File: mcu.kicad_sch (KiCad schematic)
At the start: 38 parts, among them IC1 SN74AHCT1G125DBVR, J201 Connector, USB-TYPE-C-16P, SW201 SK-12D02, U1 STM32F723VET6, U2 USBLC6-2SC6, U201 TS3USB221ARSER, X1 16MHz

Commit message: fixes & doc
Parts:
- removed C180: 1uF, PCM_JLCPCB:C_0402, symbol PCM_JLCPCB-Capacitors:0402,1uF
- removed C181: 100nF, PCM_JLCPCB:C_0402, symbol PCM_JLCPCB-Capacitors:0402,100nF

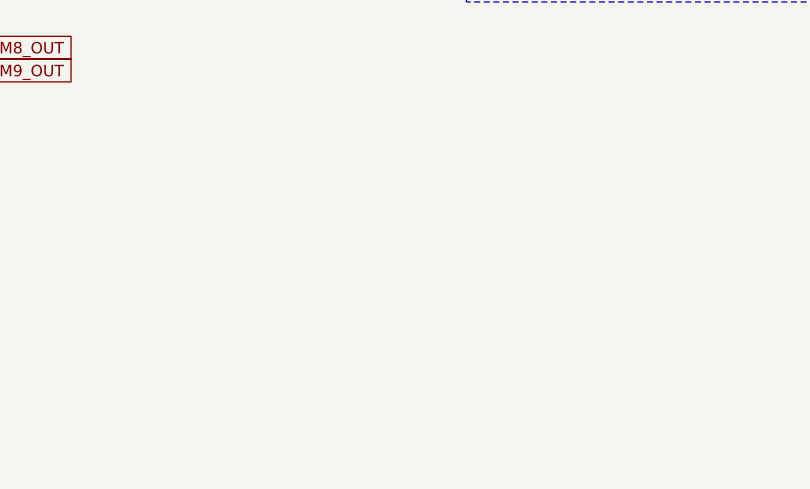
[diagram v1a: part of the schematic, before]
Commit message: Add rotary encoder symbol;
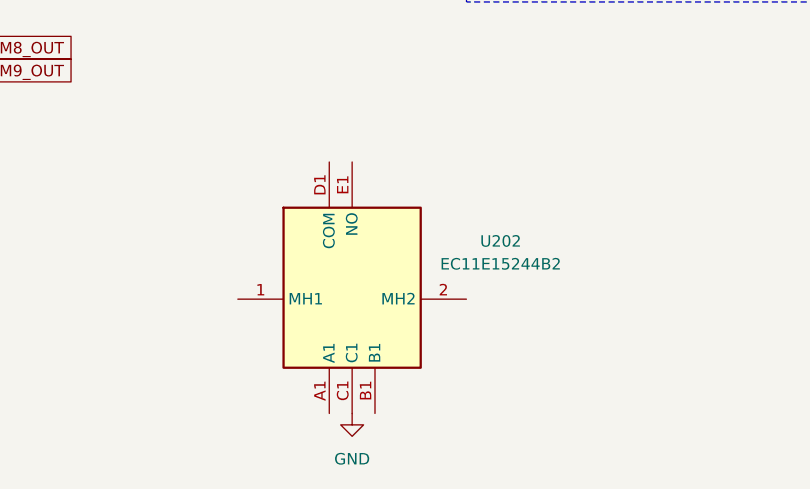
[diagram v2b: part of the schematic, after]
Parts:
- added U202: EC11E15244B2, EC11E15244B2, symbol SamacSys_Parts:EC11E15244B2
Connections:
- net GND: now also U202.C1
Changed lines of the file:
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@@
 	(symbol
 		(lib_id "power:GND")
+		(at 284.48 214.63 0)
+		(unit 1)
+		(exclude_from_sim no)
+		(in_bom yes)
+		(on_board yes)
+		(dnp no)
+		(fields_autoplaced yes)
+		(property "Reference" "#PWR0233"
+			(at 284.48 220.98 0)
+			(effects
+				(font
+					(size 1.27 1.27)
+				)
+				(hide yes)
+			)
+		)
+		(property "Value" "GND"
+			(at 284.48 219.71 0)
+			(effects
+				(font
+					(size 1.27 1.27)
+				)
+			)
+		)
+		(property "Footprint" ""
+			(at 284.48 214.63 0)
+			(effects
+				(font
+					(size 1.27 1.27)
+				)
+				(hide yes)
+			)
+		)
+		(property "Datasheet" ""
+			(at 284.48 214.63 0)
+			(effects
+				(font
+					(size 1.27 1.27)
+				)
+				(hide yes)
+			)
+		)
+		(property "Description" "Power symbol creates a global label with name \"GND\" , ground"
+			(at 284.48 214.63 0)
+			(effects
+				(font
+					(size 1.27 1.27)
+				)
+				(hide yes)
+			)
+		)
+		(pin "1"
+		)
+		(instances
+			(project "75he"
+				(path "/0edb4e17-93a4-4f7b-ad91-3a5c72b69d23/e7ec310e-33d9-421e-aaaf-42ca5ffe1b35"
+					(reference "#PWR0233")
+					(unit 1)
+				)
+			)
+		)
+	)
+	(symbol
+		(lib_id "power:GND")
 		(at 317.5 160.02 0)
 		(unit 1)
@@
 					(unit 1)
 				)
+			)
+		)
+	)
+	(symbol
+		(lib_id "SamacSys_Parts:EC11E15244B2")
+		(at 271.78 201.93 0)
+		(unit 1)
+		(exclude_from_sim no)
+		(in_bom yes)
+		(on_board yes)
+		(dnp no)
+		(fields_autoplaced yes)
+		(property "Reference" "U202"
+			(at 300.99 195.5098 0)
+			(effects
+				(font
+					(size 1.27 1.27)
+				)
+			)
+		)
+		(property "Value" "EC11E15244B2"
+			(at 300.99 198.0498 0)
+			(effects
+				(font
+					(size 1.27 1.27)
+				)
+			)
+		)
+		(property "Footprint" "EC11E15244B2"
+			(at 293.37 289.23 0)
+			(effects
+				(font
+					(size 1.27 1.27)
+				)
+				(justify left top)
+				(hide yes)
+			)
+		)
+		(property "Datasheet" "https://tech.alpsalpine.com/e/products/detail/EC11E15244B2/"
+			(at 293.37 389.23 0)
+			(effects
+				(font
+					(size 1.27 1.27)
+				)
+				(justify left top)
+				(hide yes)
+			)
+		)
+		(property "Description" "Rotary Encoder Mechanical 15 Quadrature (Incremental) Vertical"
+			(at 271.78 201.93 0)
+			(effects
+				(font
+					(size 1.27 1.27)
+				)
+				(hide yes)
+			)
+		)
+		(property "Height" "24.5"
+			(at 293.37 589.23 0)
+			(effects
+				(font
+					(size 1.27 1.27)
+				)
+				(justify left top)
+				(hide yes)
+			)
+		)
+		(property "Mouser Part Number" "688-EC11E15244B2"
+			(at 293.37 689.23 0)
+			(effects
+				(font
+					(size 1.27 1.27)
+				)
+				(justify left top)
+				(hide yes)
+			)
+		)
+		(property "Mouser Price/Stock" "https://www.mouser.co.uk/ProductDetail/Alps-Alpine/EC11E15244B2?qs=m0BA540hBPfDpUEkDmFV5A%3D%3D"
+			(at 293.37 789.23 0)
+			(effects
+				(font
+					(size 1.27 1.27)
+				)
+				(justify left top)
+				(hide yes)
+			)
+		)
+		(property "Manufacturer_Name" "ALPS Electric"
+			(at 293.37 889.23 0)
+			(effects
+				(font
+					(size 1.27 1.27)
+				)
+				(justify left top)
+				(hide yes)
+			)
+		)
+		(property "Manufacturer_Part_Number" "EC11E15244B2"
+			(at 293.37 989.23 0)
+			(effects
+				(font
+					(size 1.27 1.27)
+				)
+				(justify left top)
+				(hide yes)
+			)
+		)
+		(pin "D1"
+		)
+		(pin "A1"
+		)
+		(pin "1"
+		)
+		(pin "2"
+		)
+		(pin "B1"
+		)
+		(pin "C1"
+		)
+		(pin "E1"
+		)
+		(instances
+			(project "75he"
+				(path "/0edb4e17-93a4-4f7b-ad91-3a5c72b69d23/e7ec310e-33d9-421e-aaaf-42ca5ffe1b35"
+					(reference "U202")
+					(unit 1)
+				)

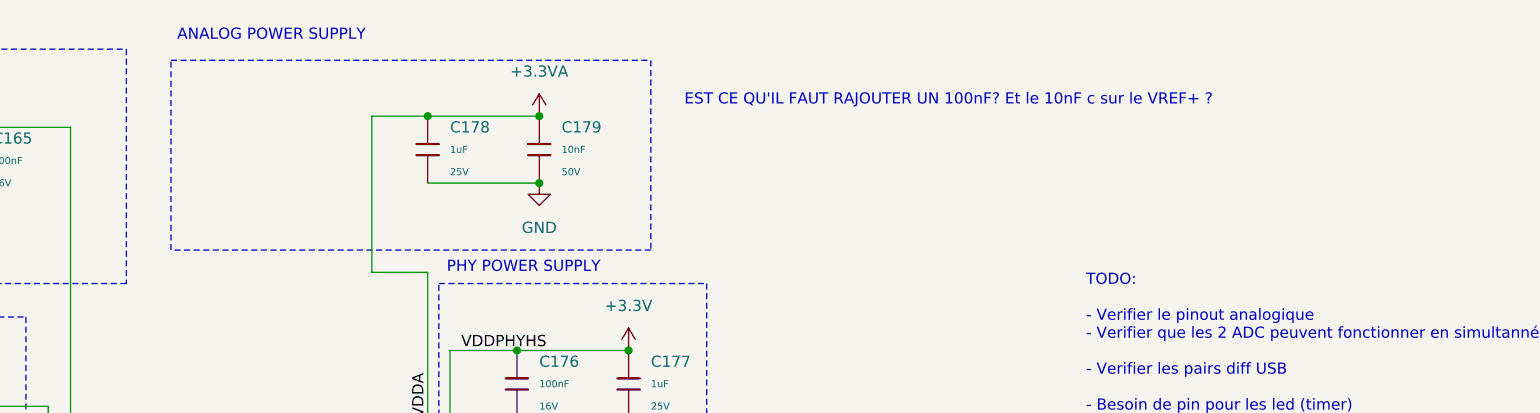
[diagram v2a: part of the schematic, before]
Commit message: adjust schematic text
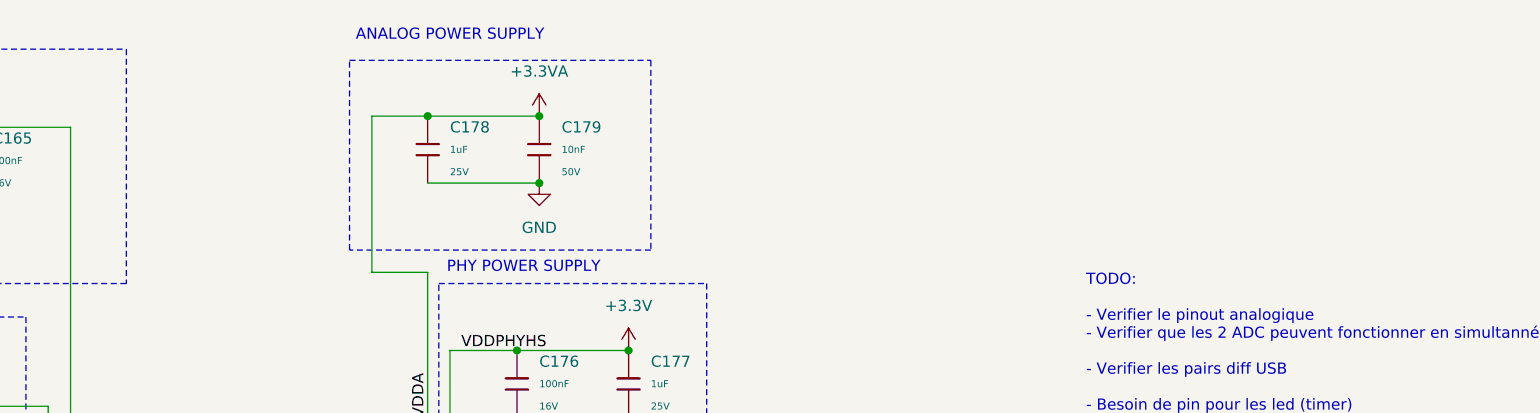
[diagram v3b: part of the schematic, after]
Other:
- note removed: "EST CE QU'IL FAUT RAJOUTER UN 100nF? Et le 10nF c sur le VREF+ ?"
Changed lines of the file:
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@@
 	)
 	(rectangle
-		(start 179.07 17.78)
+		(start 199.39 17.78)
 		(end 233.68 39.37)
 		(stroke
@@
 	(text "ANALOG POWER SUPPLY"
 		(exclude_from_sim no)
-		(at 190.5 14.986 0)
+		(at 210.82 14.986 0)
 		(effects
 			(font
@@
 		(effects
 			(font
-				(size 1.27 1.27)
-			)
-			(justify left)
-		)
-	)
-	(text "EST CE QU'IL FAUT RAJOUTER UN 100nF? Et le 10nF c sur le VREF+ ?"
-		(exclude_from_sim no)
-		(at 237.49 22.352 0)
-		(effects
-			(font

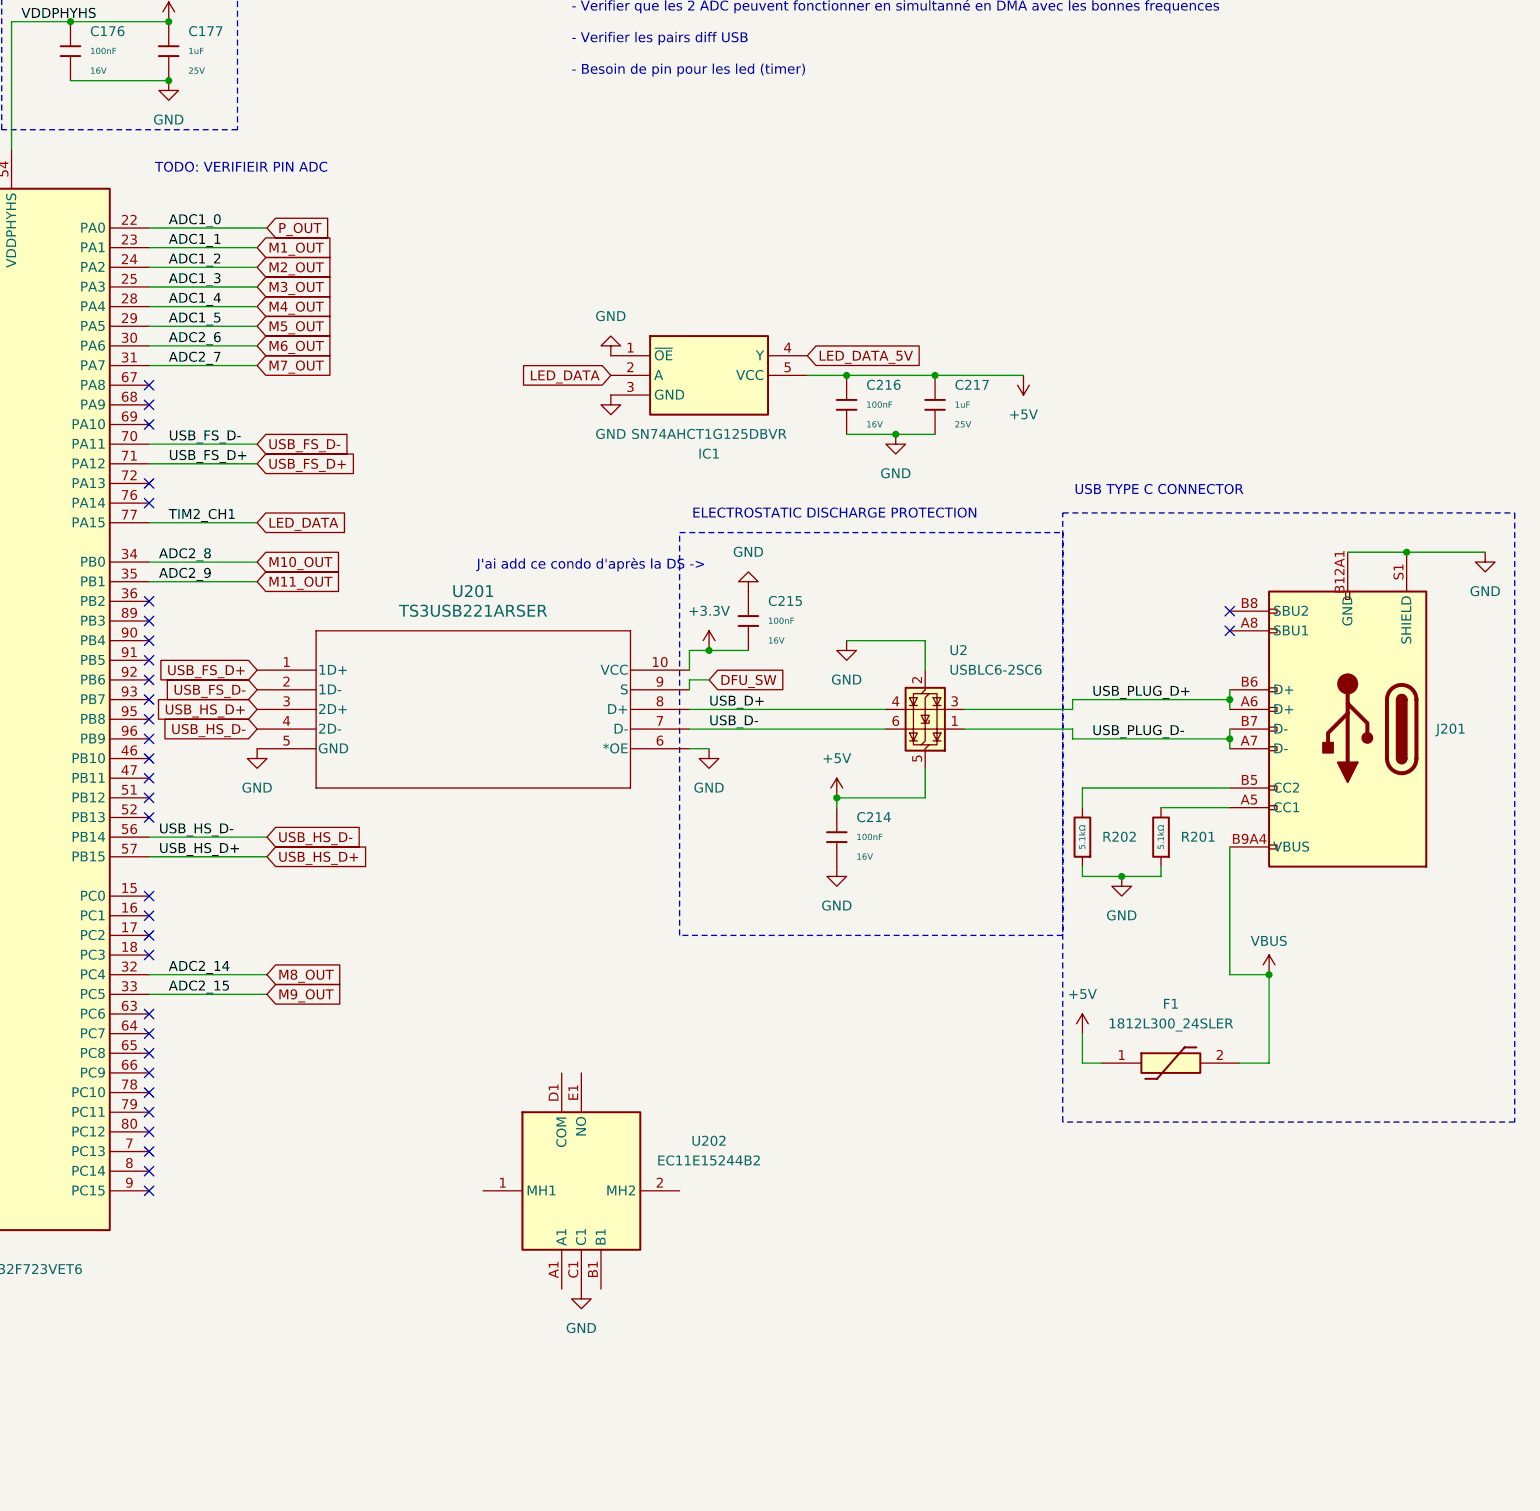
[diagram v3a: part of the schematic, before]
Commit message: encodeur ajouté
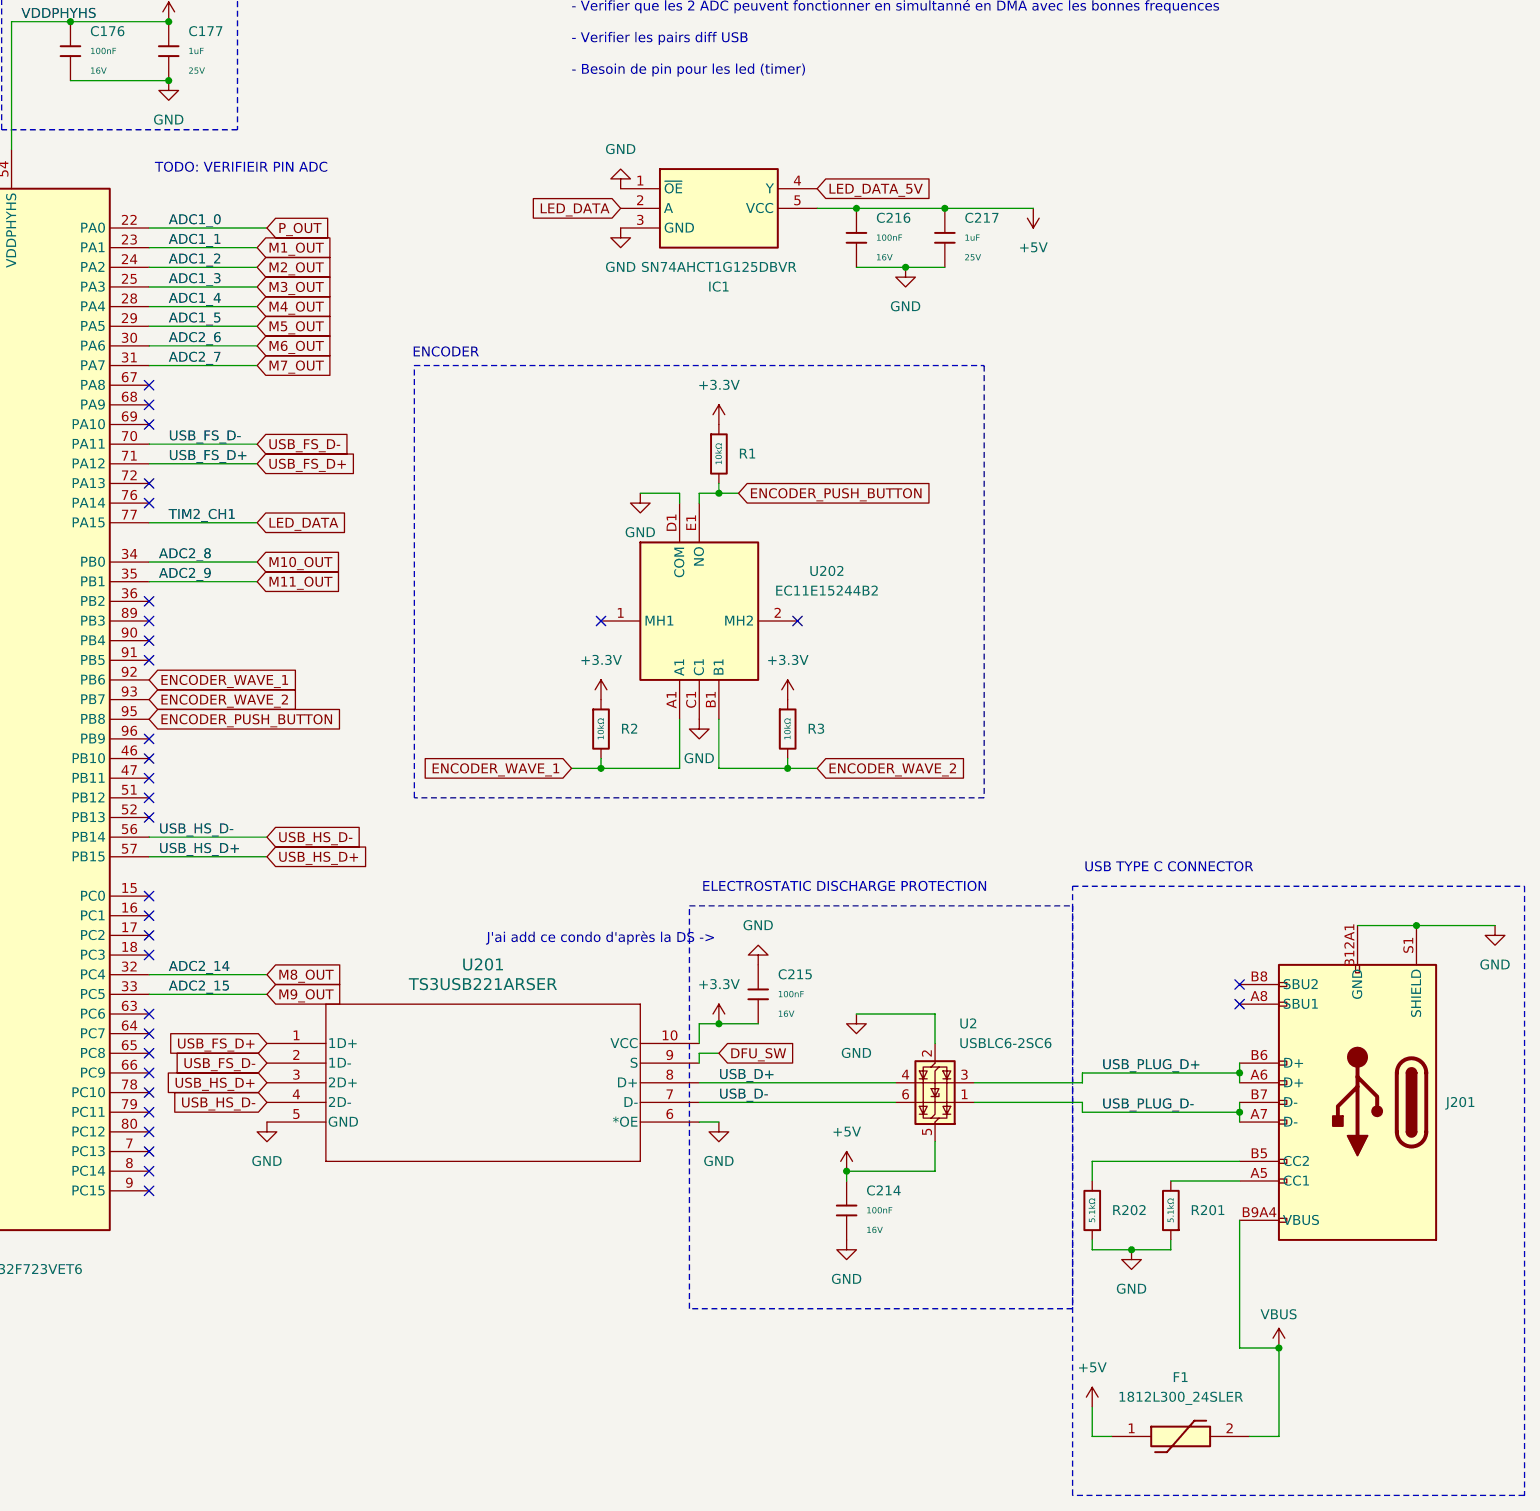
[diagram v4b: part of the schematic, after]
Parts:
- added R1, R2, R3: 10kΩ, PCM_JLCPCB:R_0402, symbol PCM_JLCPCB-Resistors:0402,10kΩ
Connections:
- net +3.3V: now also R1.1, R2.1, R3.1
- net GND: now also U202.D1 (COM)
- net ENCODER_WAVE_1: now reaches U1.92 (PB6)
- net ENCODER_WAVE_1: now also U202.A1, R2.2
- net ENCODER_WAVE_2: now reaches U1.93 (PB7)
- net ENCODER_WAVE_2: now also U202.B1, R3.2
- net ENCODER_PUSH_BUTTON: now reaches U1.95 (PB8)
- net ENCODER_PUSH_BUTTON: now also U202.E1 (NO), R1.2
- no-connect marks 59 -> 58
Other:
- note added: "ENCODER"
- moved on the sheet: C214, C215, C216, C217, F1, IC1, J201, R201, R202, U2, U201, U202

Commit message: Add WS2812 footprints, resistors and net names
Replace generic switch footprints with proper SMD components and metadata: add WS2812B RGB LED footprints (with pads, nets, 3D models and part/Datasheet/LCSC info), add many resistor footprints and detailed properties, and update net names for LED data lines (e.g. Net-(D201-DIN/DOUT) etc.). Also adjust footprint positions, pad assignments, sheet references (LED/HE Sensors), and footprint drawing/printer layers to match correct component geometry for assembly and BOM generation.
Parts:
- renumbered R2 to R286, R1 to R287, R3 to R288

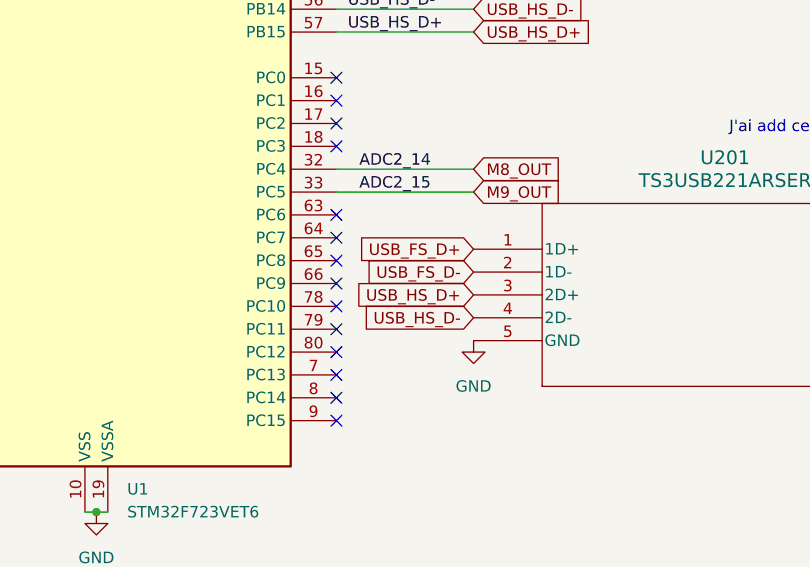
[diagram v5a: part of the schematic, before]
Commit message: Update 0402 resistors to 680Ω and add libs
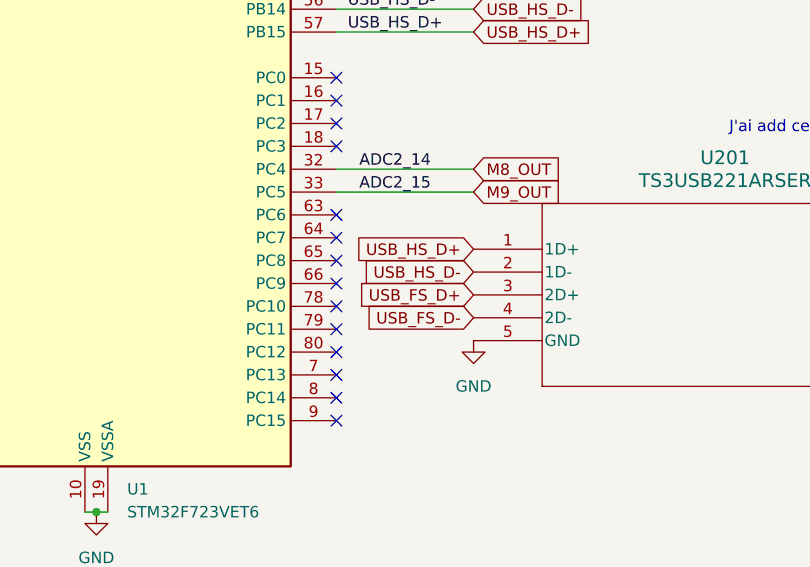
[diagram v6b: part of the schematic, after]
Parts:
- F1: footprint 1812L190SLPR -> 1812L300_24SLER:1812L190SLPR
- SW201: footprint easyeda2kicad:SW-TH_SK-12D02VG3 -> SW-TH_SK-12D02VG3:SW-TH_SK-12D02VG3; symbol easyeda2kicad:SK-12D02 -> SW-TH_SK-12D02VG3:SK-12D02
- U202: footprint EC11E15244B2 -> EC11E15244B2:EC11E15244B2
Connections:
- net USB_FS_D+: now also U201.3 (2D+); no longer U201.1 (1D+)
- net USB_FS_D-: now also U201.4 (2D-); no longer U201.2 (1D-)
- net USB_HS_D+: now also U201.1 (1D+); no longer U201.3 (2D+)
- net USB_HS_D-: now also U201.2 (1D-); no longer U201.4 (2D-)
